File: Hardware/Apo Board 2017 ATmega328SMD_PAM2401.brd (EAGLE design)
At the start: 85.1 x 52.7 mm, 38 parts, among them Q1 RESONATORSMD, U1 LED-TRICOLOR-5050-IC, U10 LED-TRICOLOR-5050-IC, U11 LED-TRICOLOR-5050-IC, U13 ATMEGA328, U2 PAM2401, U3 LED-TRICOLOR-5050-IC, U4 LED-TRICOLOR-5050-IC, U5 LED-TRICOLOR-5050-IC, U6 LED-TRICOLOR-5050-IC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

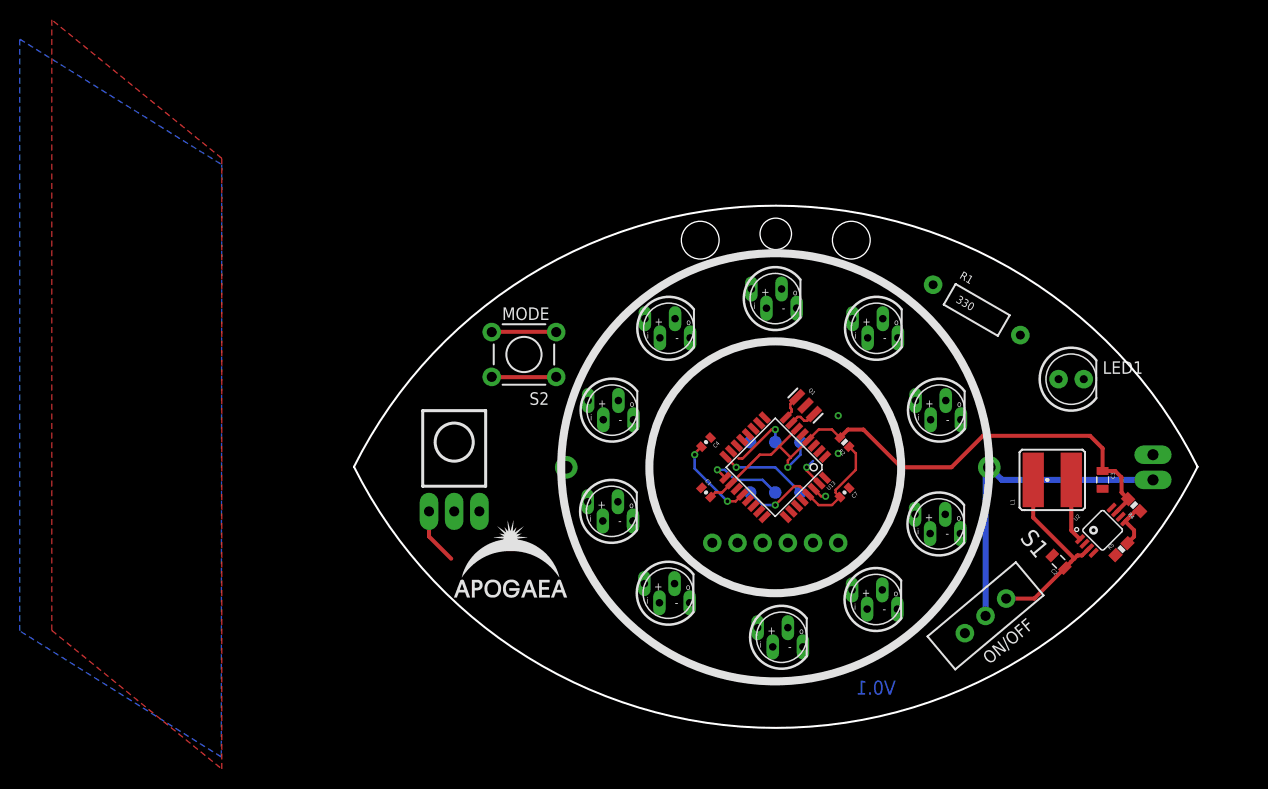
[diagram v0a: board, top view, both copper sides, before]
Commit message: Added Deacon board files. finished prelim layout
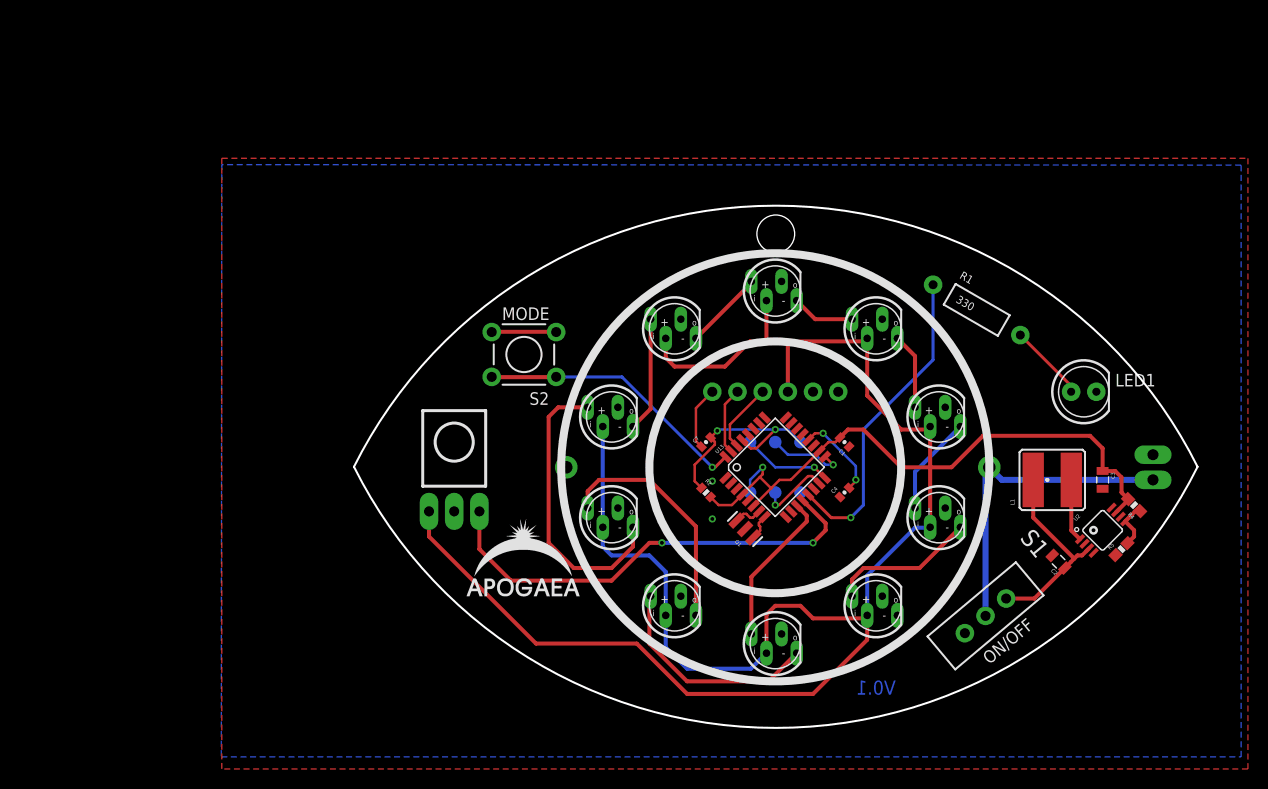
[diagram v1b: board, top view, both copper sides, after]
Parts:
- moved LOGO1 52.9 mm to (0.05, -24.1)
- moved U7 28.7 mm to (0.00, -17.8)
- moved U11 28.7 mm to (0.00, 17.8)
- moved U1 28.3 mm to (16.5, -5.08)
- moved U8 28.3 mm to (10.2, -14.0)
- moved U3 28.2 mm to (-16.5, 5.08)
- moved U6 28.0 mm to (-10.2, -14.0)
- moved U4 28.0 mm to (-10.2, 14.0)
- moved U5 27.6 mm to (-16.5, -5.08)
- moved U9 27.3 mm to (16.5, 5.08)
- moved U10 27.3 mm to (10.2, 14.0)
- moved JP4 19.8 mm to (-6.35, 7.62), turned to 180 degrees
- moved C1 14.9 mm to (6.99, 2.54), turned to 135 degrees
- moved C4 14.9 mm to (6.99, -2.54), turned to 45 degrees
- moved C7 14.9 mm to (-6.99, 2.54), turned to 45 degrees
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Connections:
- net BUTTON: now also U13.32; no longer U13.14
- net IR_RX: now also U13.12; no longer U13.13
- net IR_TX: now also U13.13; no longer U13.12
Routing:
- net +5V: track 68.5 -> 254.6 mm
- net IR_RX: track 0.00 -> 46.2 mm, vias 0 -> 2
- net IR_TX: track 0.00 -> 32.2 mm, vias 0 -> 1
- net N$5: track 0.00 -> 29.4 mm
- net N$2: track 0.00 -> 24.0 mm
- net N$1: track 0.00 -> 22.4 mm
- net BUTTON: track 6.50 -> 27.8 mm, vias 0 -> 1
- net LED_PIN: track 0.00 -> 15.7 mm
- net N$14: track 0.00 -> 14.8 mm
- net N$6: track 0.00 -> 11.6 mm
- net N$13: track 0.00 -> 10.1 mm
- net DOUT_DIN: track 0.00 -> 8.06 mm
- net N$3: track 0.00 -> 7.84 mm
- net N$11: track 0.00 -> 7.69 mm
- net DTR: track 0.00 -> 6.45 mm
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
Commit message: Final touches before review
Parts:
- added C6: (no value), SparkFun-Capacitors:CAP-PTH-SMALL
- added R3: 100k, SparkFun-Resistors:0603-RES
- moved C3 2.01 mm to (32.4, -3.17), turned to 225 degrees
- moved U2 1.80 mm to (31.8, -7.62)
- moved R4 1.80 mm to (34.9, -5.08)
- moved L1 1.80 mm to (26.7, -2.54), turned to 45 degrees
- moved C2 1.80 mm to (27.3, -10.8)
- moved R5 1.80 mm to (33.7, -9.53)
- moved TP1 1.27 mm to (-2.54, -1.27)
- moved TP2 1.27 mm to (0.00, -1.27)
- moved TP3 1.27 mm to (2.54, -1.27)
- moved TP4 1.27 mm to (-2.54, 1.27)
- moved TP5 1.27 mm to (0.00, 1.27)
- moved TP6 1.27 mm to (2.54, 1.27)
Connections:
- new net N$4: R3.2, U2.6
- net +5V: now also C6.1
- net GND: now also C6.2, R3.1
- net N$10: now also U2.2
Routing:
- net N$4: track 0.00 -> 5.43 mm
- net N$10: track 20.1 -> 22.1 mm
- net +5V: track 254.6 -> 253.0 mm
- net MOSI: track 7.23 -> 5.96 mm
- net RESET: track 20.8 -> 22.0 mm
- net SCK: track 7.95 -> 7.44 mm
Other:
- board text added: "3)Press button to share mode"
- board text added: "4)Collect as many modes as you can"
- board text added: "5V"
- board text added: "GND"
- board text added: "How to Play: 1)Two Eyeballs see one another 2)LEDs start pulsing"
- board text added: "MISO"
- board text added: "MOSI"
- board text added: "OFF/ON"
- board text added: "RST"
- board text added: "SCK"
- board text added: "SOLDER ON THIS SIDE"
- board text removed: "ON/OFF"

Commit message: Fixing Natural Jumper and few moonier text tweaks
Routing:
- net +5V: track 253.0 -> 252.0 mm
- net N$10: track 22.1 -> 23.0 mm
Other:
- board text added: "BLK-"
- board text added: "RED+"
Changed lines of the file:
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@@
 <?xml version="1.0" encoding="utf-8"?>
 <!DOCTYPE eagle SYSTEM "eagle.dtd">
-<eagle version="7.3.0">
+<eagle version="7.6.0">
 <drawing>
 <settings>
@@
 <layer number="20" name="Dimension" color="15" fill="1" visible="yes" active="yes"/>
 <layer number="21" name="tPlace" color="16" fill="1" visible="yes" active="yes"/>
-<layer number="22" name="bPlace" color="14" fill="1" visible="no" active="yes"/>
+<layer number="22" name="bPlace" color="14" fill="1" visible="yes" active="yes"/>
 <layer number="23" name="tOrigins" color="15" fill="1" visible="yes" active="yes"/>
-<layer number="24" name="bOrigins" color="15" fill="1" visible="no" active="yes"/>
-<layer number="25" name="tNames" color="7" fill="1" visible="yes" active="yes"/>
+<layer number="24" name="bOrigins" color="15" fill="1" visible="yes" active="yes"/>
+<layer number="25" name="tNames" color="7" fill="1" visible="no" active="yes"/>
 <layer number="26" name="bNames" color="7" fill="1" visible="no" active="yes"/>
 <layer number="27" name="tValues" color="7" fill="1" visible="no" active="yes"/>
@@
 <layer number="43" name="vRestrict" color="2" fill="10" visible="no" active="yes"/>
 <layer number="44" name="Drills" color="7" fill="1" visible="no" active="yes"/>
-<layer number="45" name="Holes" color="7" fill="1" visible="no" active="yes"/>
+<layer number="45" name="Holes" color="7" fill="1" visible="yes" active="yes"/>
 <layer number="46" name="Milling" color="3" fill="1" visible="no" active="yes"/>
 <layer number="47" name="Measures" color="7" fill="1" visible="no" active="yes"/>
 <layer number="48" name="Document" color="7" fill="1" visible="no" active="yes"/>
-<layer number="49" name="Reference" color="13" fill="1" visible="no" active="yes"/>
+<layer number="49" name="Reference" color="13" fill="1" visible="yes" active="yes"/>
 <layer number="50" name="dxf" color="7" fill="1" visible="no" active="yes"/>
-<layer number="51" name="tDocu" color="6" fill="1" visible="no" active="yes"/>
+<layer number="51" name="tDocu" color="6" fill="1" visible="yes" active="yes"/>
 <layer number="52" name="bDocu" color="7" fill="1" visible="no" active="yes"/>
 <layer number="53" name="tGND_GNDA" color="7" fill="9" visible="no" active="no"/>
@@
 <text x="-13.843" y="-13.97" size="0.9398" layer="22" font="vector" ratio="15" rot="MR0">3)Press button to
 share mode</text>
+<text x="39.37" y="-3.81" size="1.016" layer="22" font="vector" ratio="15" rot="MR0">RED+</text>
+<text x="39.37" y="2.54" size="1.016" layer="22" font="vector" ratio="15" rot="MR0">BLK-</text>
 </plain>
 <attributes>
@@
 <wire x1="9.271" y1="-17.399" x2="9.271" y2="-14.9384" width="0.4064" layer="1"/>
 <contactref element="C6" pad="1"/>
-<wire x1="31.115" y1="3.175" x2="20.955" y2="3.175" width="0.4064" layer="1"/>
-<wire x1="31.115" y1="3.175" x2="31.75" y2="2.54" width="0.4064" layer="1"/>
-<wire x1="31.75" y1="2.54" x2="31.75" y2="0.635" width="0.4064" layer="1"/>
-<wire x1="33.655" y1="0.635" x2="31.75" y2="0.635" width="0.4064" layer="1"/>
 <wire x1="34.32395625" y1="-4.47895625" x2="33.8074" y2="-3.9624" width="0.4064" layer="1"/>
 <wire x1="33.8074" y1="-3.9624" x2="33.8074" y2="-3.324609375" width="0.4064" layer="1"/>
 <wire x1="33.8074" y1="-3.324609375" x2="33.02139375" y2="-2.538603125" width="0.4064" layer="1"/>
 <wire x1="33.02139375" y1="-2.538603125" x2="33.018603125" y2="-2.538603125" width="0.4064" layer="1"/>
-<wire x1="33.018603125" y1="-2.538603125" x2="31.75" y2="-1.27" width="0.4064" layer="1"/>
-<wire x1="31.75" y1="-1.27" x2="31.75" y2="0.635" width="0.4064" layer="1"/>
 <wire x1="-3.31816875" y1="-2.75248125" x2="-1.8356875" y2="-1.27" width="0.254" layer="1"/>
 <wire x1="-1.8356875" y1="-1.27" x2="-1.27" y2="-1.27" width="0.254" layer="1"/>
@@
 <wire x1="34.32395625" y1="-4.586421875" x2="34.323959375" y2="-4.58641875" width="0.3048" layer="1"/>
 <wire x1="34.323959375" y1="-4.58641875" x2="34.32395625" y2="-4.47895625" width="0.3048" layer="1"/>
+<wire x1="33.018603125" y1="-2.538603125" x2="31.115" y2="-0.635" width="0.4064" layer="1"/>
+<wire x1="31.115" y1="-0.635" x2="27.305" y2="3.175" width="0.4064" layer="1"/>
+<wire x1="27.305" y1="3.175" x2="20.955" y2="3.175" width="0.4064" layer="1"/>
+<wire x1="33.655" y1="0.635" x2="32.385" y2="0.635" width="0.4064" layer="1"/>
+<wire x1="32.385" y1="0.635" x2="31.115" y2="-0.635" width="0.4064" layer="1"/>
 </signal>
 <signal name="TX">
@@
 <contactref element="U2" pad="2"/>
 <wire x1="28.8925" y1="-10.4775" x2="27.94139375" y2="-11.42860625" width="0.4064" layer="1"/>
-<wire x1="29.9292" y1="-8.981178125" x2="30.38881875" y2="-9.440796875" width="0.4064" layer="1"/>
 <wire x1="22.86" y1="-4.445" x2="22.86" y2="-3.63470625" width="0.4064" layer="1"/>
 <wire x1="22.86" y1="-3.63470625" x2="25.312353125" y2="-1.182353125" width="0.4064" layer="1"/>
 <wire x1="27.94139375" y1="-11.43139375" x2="27.94139375" y2="-11.42860625" width="0.3048" layer="1"/>
+<wire x1="29.9292" y1="-8.981178125" x2="29.21" y2="-9.700378125" width="0.4064" layer="1"/>
+<wire x1="29.21" y1="-9.700378125" x2="29.21" y2="-10.16" width="0.4064" layer="1"/>
 </signal>
 <signal name="N$12">

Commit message: Final version for Prototypes V0.1 and GERBERS
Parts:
- added U$1, U$2: (no value), Openponics:APOLOGO
- C6: device SparkFun-Capacitors:CAP-PTH-SMALL -> SparkFun-Capacitors:1206
- U1: value LED-TRICOLOR-5050-IC -> PAM2401; device SparkFun-LED:LED-RGB-THRU -> SparkFun-PowerIC:MSOP8
- U2: value PAM2401 -> LED-TRICOLOR-5050-IC; device SparkFun-PowerIC:MSOP8 -> SparkFun-LED:LED-RGB-THRU
- moved U1 15.5 mm to (31.8, -7.62), turned to 315 degrees
- moved U2 15.5 mm to (16.5, -5.08), turned to 180 degrees
- moved C4 7.47 mm to (5.71, 4.83), turned to 225 degrees
- moved C6 1.09 mm to (32.6, 0.25), turned to 45 degrees
- moved U7 0.89 mm to (0.00, -16.9)
- moved C3 0.36 mm to (32.6, -2.92)
- renumbered JP1 to U12
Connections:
- net N$7 renamed +BATT_RAW
- net +5V: now also U1.7, U2.2; no longer U1.2, U2.7
- net GND: now also U1.4, U1.8, U2.3; no longer U1.3, U2.4, U2.8
- net N$10: now also U1.2, U1.3; no longer U2.2, U2.3
- net N$12: now also U1.5; no longer U2.5
- net N$13: now also U2.1; no longer U1.1
- net N$14: now also U2.4; no longer U1.4
- net N$4: now also U1.6; no longer U2.6
- net N$8: now also U1.1; no longer U2.1
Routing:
- net +5V: track 252.0 -> 219.1 mm
- net AREF: track 8.95 -> 2.61 mm, vias 2 -> 0
- net N$2: track 24.0 -> 18.4 mm
- net IR_TX: track 32.2 -> 28.7 mm
- net N$14: track 14.8 -> 17.1 mm
- net IR_RX: track 46.2 -> 44.5 mm
- net N$9: track 6.36 -> 8.01 mm
- net N$1: track 22.4 -> 23.6 mm
- net N$13: track 10.1 -> 11.2 mm
- net N$11: track 7.69 -> 8.80 mm
- net N$6: track 11.6 -> 10.6 mm
- net N$5: track 29.4 -> 28.9 mm
- net DOUT_DIN: track 8.06 -> 7.51 mm
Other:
- board text added: "3) Press button to share mode"
- board text added: "4) Collect as many modes as you can"
- board text added: "How to Play: 1) Two Eyeballs see one another 2) LEDs start pulsing"
- board text removed: "3)Press button to share mode"
- board text removed: "4)Collect as many modes as you can"
- board text removed: "How to Play: 1)Two Eyeballs see one another 2)LEDs start pulsing"
